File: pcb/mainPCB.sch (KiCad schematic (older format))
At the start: 31 parts, among them J1 Inputs, J11 Conn_01x04_Male, J12 Conn_01x04_Male, J2 ESP32_left, J3 ESP32_right, J4 F9P_left_top, J5 F9P left bottom, J6 F9P right, J7 Motor A, J8 Motor B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

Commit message: first version of the new feature set
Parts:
- removed C1: 100n, symbol Device:C
- removed C10: 10u, symbol Device:C
- removed C14: 470u, symbol Device:CP
- removed J1: Inputs, symbol Connector:Screw_Terminal_01x08
- removed J11, J12: Conn_01x04_Male, symbol Connector:Conn_01x04_Male
- removed J2: ESP32_left, symbol Connector:Conn_01x15_Female
- removed J3: ESP32_right, symbol Connector:Conn_01x15_Female
- removed J4: F9P_left_top, symbol Connector:Conn_01x08_Female
- removed J5: F9P left bottom, symbol Connector:Conn_01x08_Female
- removed J6: F9P right, symbol Connector:Conn_01x08_Female
- removed J7: Motor A, symbol Connector:Screw_Terminal_01x02
- removed J8: Motor B, symbol Connector:Screw_Terminal_01x02
- removed J9: Power, symbol Connector:Screw_Terminal_01x02
- removed U1: MMA8452Q, symbol Sensor_Motion_own:MMA8452Q
- added C5: 22u, Capacitor_SMD:C_0805_2012Metric, symbol Device:C
- added D3: LED/green, Capacitor_SMD:C_0805_2012Metric, symbol Device:LED
- added D4: LED/red, Capacitor_SMD:C_0805_2012Metric, symbol Device:LED
- added H6, H7, H8: MountingHole, MountingHole:MountingHole_3.2mm_M3_DIN965, symbol Mechanical:MountingHole
- added IC1: FXL6408UMX, ICs_own:QFN40P180X260X55-16N, symbol Interface_Expansion_own:FXL6408UMX
- added J1: PTSM-Header-Horizontal-6, Connector_own:1814883, symbol Connector_own:PTSM-Header-Horizontal-6
- added J3: PTSM-Header-Horizontal-7, Connector_own:1814896, symbol Connector_own:PTSM-Header-Horizontal-7
- added J4: CCA-Header-Horizontal-4, Connector_own:1836366, symbol Connector_own:CCA-Header-Horizontal-4
- added R10, R6: 47k, Resistor_SMD:R_0805_2012Metric, symbol Device:R
- added R11, R12, R13, R7, R8, R9: 1k, Resistor_SMD:R_0805_2012Metric, symbol Device:R
- added SW1: SW_Push, Button_Switch_SMD:SW_SPST_PTS645, symbol Switch:SW_Push
- added U1: ESP32-WROOM-32, RF_Module:ESP32-WROOM-32, symbol RF_Module:ESP32-WROOM-32
- C1: renamed from C11; value 22n -> 100n; footprint (none) -> Capacitor_SMD:C_0805_2012Metric
- C2: value 4.7u -> 100n; footprint (none) -> Capacitor_SMD:C_0805_2012Metric
- C3: footprint (none) -> Capacitor_SMD:C_0805_2012Metric
- C4: value 22u -> 100n; footprint (none) -> Capacitor_SMD:C_0805_2012Metric
- D1: value Network -> LED/blue; footprint (none) -> Capacitor_SMD:C_0805_2012Metric
- D2: value NTRIP -> LED/blue; footprint (none) -> Capacitor_SMD:C_0805_2012Metric
- H1: renamed from H5; footprint (none) -> MountingHole:MountingHole_4.3mm_M4_DIN965
- H2: footprint (none) -> MountingHole:MountingHole_4.3mm_M4_DIN965
- H3: renamed from H4; footprint (none) -> MountingHole:MountingHole_4.3mm_M4_DIN965
- H4: renamed from H3; footprint (none) -> MountingHole:MountingHole_4.3mm_M4_DIN965
- H5: renamed from H1; footprint (none) -> MountingHole:MountingHole_3.2mm_M3_DIN965
- R1: value 47 -> 120; footprint (none) -> Resistor_SMD:R_0805_2012Metric
- R2, R3: value 160 -> 620; footprint (none) -> Resistor_SMD:R_0805_2012Metric
- R4, R5: value 4.7k -> 620; footprint (none) -> Resistor_SMD:R_0805_2012Metric
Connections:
- net labels added: CAN_RXD, CAN_TXD, ESP_EN, I2C_3_SCL, I2C_3_SDA, I2C_5_SCL, I2C_5_SDA, M1_INA, M1_INB, M1_PWM, M2_INA, M2_INB, M2_PWM, RXD01, RXD02, TXD01, TXD02
- net labels removed: +3.3V, CAN_RX, CAN_TX, I2C_SCL, I2C_SDA, VSPI_CLK, VSPI_CS0, VSPI_MISO, VSPI_MOSI
- wire segments 137 -> 187
- no-connect marks 31 -> 9
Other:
- note removed: "Extensions"
- moved on the sheet: C1, H1, H2, H3, H4, H5, R1

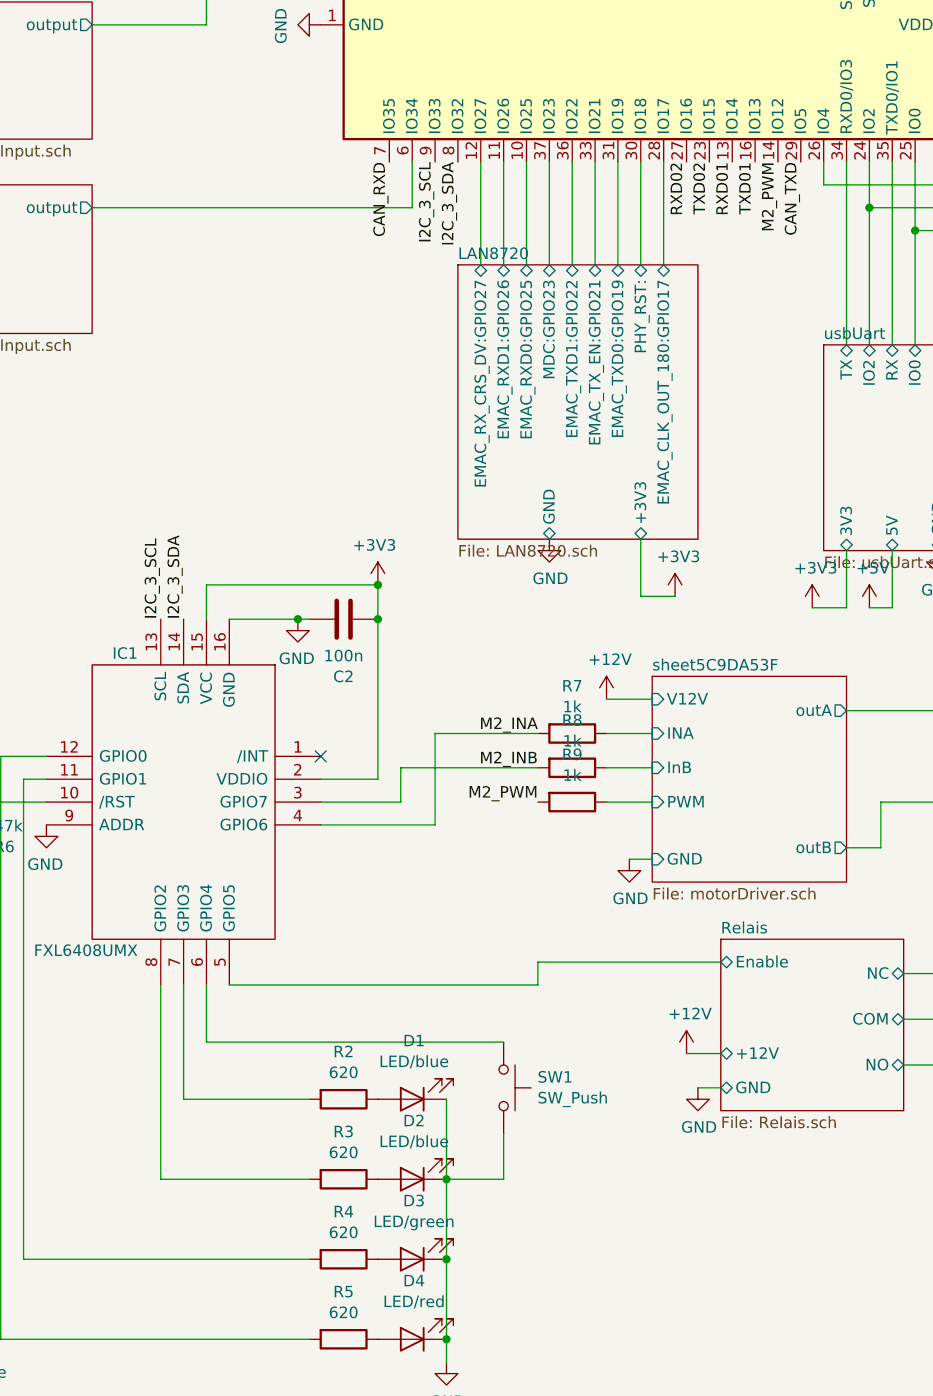
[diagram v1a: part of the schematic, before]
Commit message: changed connection of the LAN8720A, RST to the FXL6408 and MDIO to the ESP32 (where RST was before). fixes #2
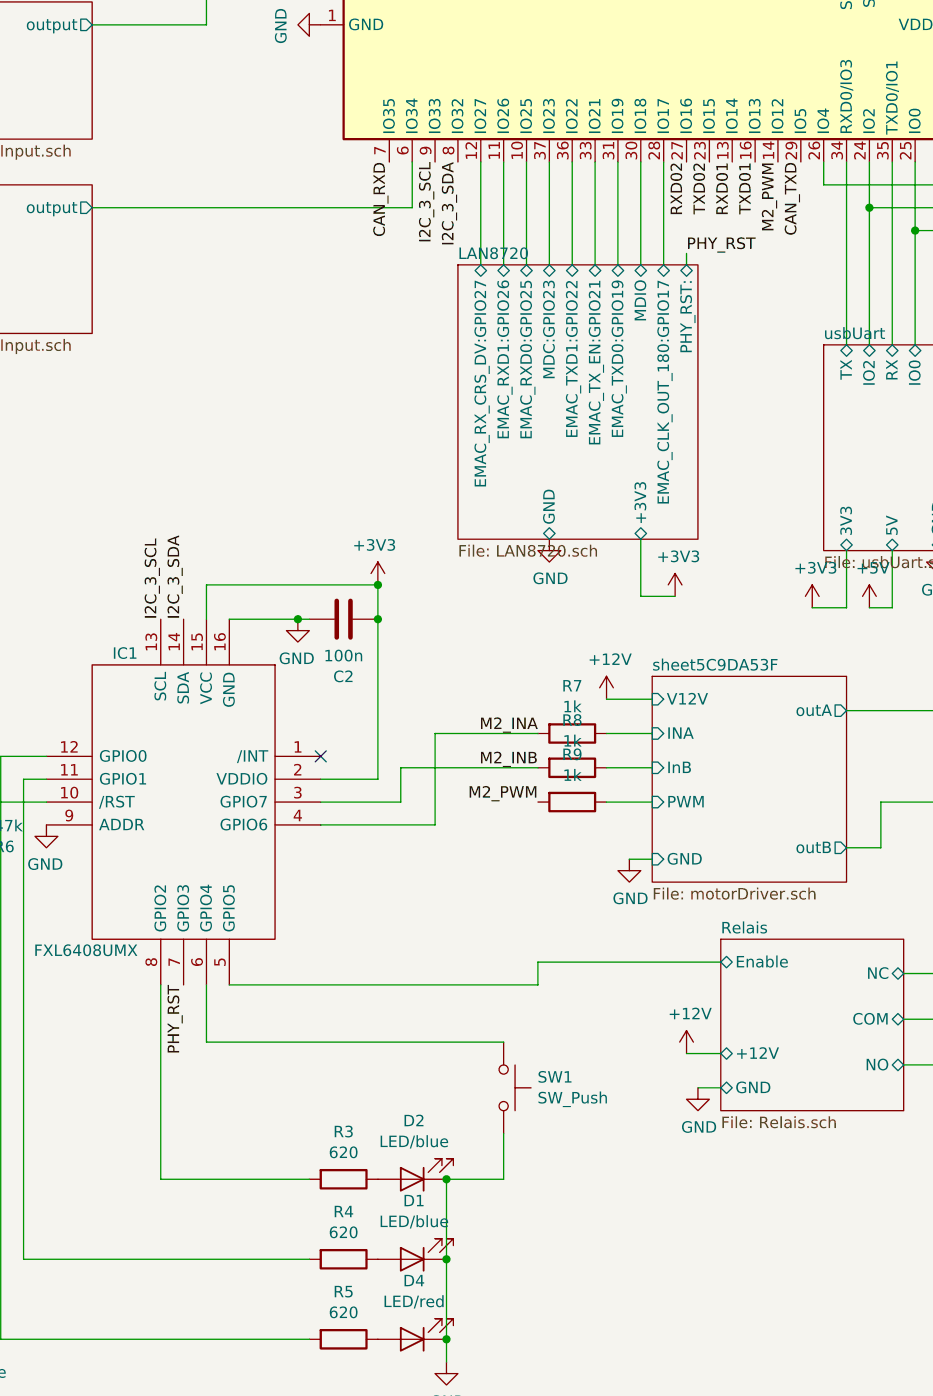
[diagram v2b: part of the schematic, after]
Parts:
- removed D1: LED/blue, Capacitor_SMD:C_0805_2012Metric, symbol Device:LED
- removed R2: 620, Resistor_SMD:R_0805_2012Metric, symbol Device:R
- D1: renamed from D3; value LED/green -> LED/blue
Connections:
- net PHY_RST: now reaches IC1.7 (GPIO3)
- net LAN8720/PHY_RST: renamed LAN8720/MDIO
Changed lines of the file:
@@
 	7100 4150 7000 4150
-$Comp
-L Device:R R2
-U 1 1 5CB615BA
-P 4700 6300
-F 0 "R2" V 4493 6300 50  0000 C CNN
-F 1 "620" V 4584 6300 50  0000 C CNN
-F 2 "Resistor_SMD:R_0805_2012Metric" V 4630 6300 50  0001 C CNN
-F 3 "~" H 4700 6300 50  0001 C CNN
-	1    4700 6300
-	0    1    1    0
-$EndComp
-$Comp
-L Device:LED D1
-U 1 1 5CB66F82
-P 5000 6300
-F 0 "D1" H 4992 6045 50  0000 C CNN
-F 1 "LED/blue" H 4992 6136 50  0000 C CNN
-F 2 "Capacitor_SMD:C_0805_2012Metric" H 5000 6300 50  0001 C CNN
-F 3 "~" H 5000 6300 50  0001 C CNN
-	1    5000 6300
-	-1   0    0    1
-$EndComp
 $Comp
 L Mechanical:MountingHole H8
@@
 F5 "EMAC_TX_EN:GPIO21" B T 5800 2650 50
 F6 "+3V3" B B 6000 3850 50
-F7 "PHY_RST:" B T 6000 2650 50
+F7 "PHY_RST:" B T 6200 2650 50
 F8 "MDC:GPIO23" B T 5600 2650 50
 F9 "GND" B B 5600 3850 50
@@
 F11 "EMAC_RXD0:GPIO25" B T 5500 2650 50
 F12 "EMAC_RXD1:GPIO26" B T 5400 2650 50
+F13 "MDIO" B T 6000 2650 50
 $EndSheet
 Wire Wire Line
@@
 Wire Wire Line
 	6100 2200 6100 2650
-Wire Wire Line
-	6000 2650 6000 2200
 Wire Wire Line
 	5900 2200 5900 2650
@@
 $EndComp
 $Comp
-L Device:LED D3
+L Device:LED D1
 U 1 1 5CF2F275
 P 5000 7000
-F 0 "D3" H 4992 6745 50  0000 C CNN
-F 1 "LED/green" H 4992 6836 50  0000 C CNN
+F 0 "D1" H 4992 6745 50  0000 C CNN
+F 1 "LED/blue" H 4992 6836 50  0000 C CNN
 F 2 "Capacitor_SMD:C_0805_2012Metric" H 5000 7000 50  0001 C CNN
 F 3 "~" H 5000 7000 50  0001 C CNN
@@
 	-1   0    0    1
 $EndComp
-Wire Wire Line
-	5150 6300 5150 6650
 Connection ~ 5150 6650
 Wire Wire Line
@@
 	1    0    0    -1
 $EndComp
-Wire Wire Line
-	4550 6300 4000 6300
 Wire Wire Line
 	3900 6650 4550 6650
@@
 	4100 5800 4100 6050
 Wire Wire Line
-	4000 5800 4000 6300
-Wire Wire Line
 	3900 5800 3900 6650
 Wire Wire Line
@@
 Wire Wire Line
 	5100 5100 4600 5100
+Wire Wire Line
+	6000 2200 6000 2650
+Text Label 4000 5800 3    50   ~ 0
+PHY_RST
+Text Label 6200 2600 0    50   ~ 0
+PHY_RST
+Wire Wire Line
+	6200 2600 6200 2650
 $EndSCHEMATC

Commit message: Added an other uart for ardusimple RTK2Bligh daughterboard on top of the normal RTK2B. Removed two LEDs to free up PINs
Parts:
- removed D1: LED/blue, Capacitor_SMD:C_0805_2012Metric, symbol Device:LED
- removed D4: LED/red, Capacitor_SMD:C_0805_2012Metric, symbol Device:LED
- removed R4, R5: 620, Resistor_SMD:R_0805_2012Metric, symbol Device:R
- added J2: Conn_01x02_Male, Connector_PinHeader_2.54mm:PinHeader_1x02_P2.54mm_Vertical, symbol Connector:Conn_01x02_Male
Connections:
- net M1_INA: now also IC1.4 (GPIO6); no longer U1.25 (IO0)
- net M1_INB: now also IC1.3 (GPIO7); no longer U1.24 (IO2)
- net M2_INA: now also IC1.6 (GPIO4); no longer IC1.4 (GPIO6)
- net M2_INB: now also IC1.5 (GPIO5); no longer IC1.3 (GPIO7)
- net PHY_RST: now also IC1.11 (GPIO1); no longer IC1.7 (GPIO3)
- net Relais/Enable: now also IC1.7 (GPIO3); no longer IC1.5 (GPIO5)
- net at SW1.1: now also IC1.12 (GPIO0); no longer IC1.6 (GPIO4)
- new net RXD03: J2.2 (Pin_2), U1.24 (IO2)
- new net TXD03: J2.1 (Pin_1), U1.25 (IO0)
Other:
- moved on the sheet: SW1
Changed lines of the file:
@@
 	6800 2300 8800 2300
 Wire Wire Line
-	8800 2300 8800 5100
-Wire Wire Line
-	8700 2400 8700 5400
-Wire Wire Line
-	8700 5400 8750 5400
-Wire Wire Line
-	7200 2500 8600 2500
-Wire Wire Line
-	8600 2500 8600 5700
-Wire Wire Line
-	8600 5700 8700 5700
+	7200 2500 7900 2500
 Connection ~ 7200 2500
 Wire Wire Line
@@
 	-1   0    0    1
 $EndComp
-$Comp
-L Device:R R4
-U 1 1 5CF2F26E
-P 4700 7000
-F 0 "R4" V 4493 7000 50  0000 C CNN
-F 1 "620" V 4584 7000 50  0000 C CNN
-F 2 "Resistor_SMD:R_0805_2012Metric" V 4630 7000 50  0001 C CNN
-F 3 "~" H 4700 7000 50  0001 C CNN
-	1    4700 7000
-	0    1    1    0
-$EndComp
-$Comp
-L Device:LED D1
-U 1 1 5CF2F275
-P 5000 7000
-F 0 "D1" H 4992 6745 50  0000 C CNN
-F 1 "LED/blue" H 4992 6836 50  0000 C CNN
-F 2 "Capacitor_SMD:C_0805_2012Metric" H 5000 7000 50  0001 C CNN
-F 3 "~" H 5000 7000 50  0001 C CNN
-	1    5000 7000
-	-1   0    0    1
-$EndComp
-$Comp
-L Device:R R5
-U 1 1 5CF379C3
-P 4700 7350
-F 0 "R5" V 4493 7350 50  0000 C CNN
-F 1 "620" V 4584 7350 50  0000 C CNN
-F 2 "Resistor_SMD:R_0805_2012Metric" V 4630 7350 50  0001 C CNN
-F 3 "~" H 4700 7350 50  0001 C CNN
-	1    4700 7350
-	0    1    1    0
-$EndComp
-$Comp
-L Device:LED D4
-U 1 1 5CF379CA
-P 5000 7350
-F 0 "D4" H 4992 7095 50  0000 C CNN
-F 1 "LED/red" H 4992 7186 50  0000 C CNN
-F 2 "Capacitor_SMD:C_0805_2012Metric" H 5000 7350 50  0001 C CNN
-F 3 "~" H 5000 7350 50  0001 C CNN
-	1    5000 7350
-	-1   0    0    1
-$EndComp
-Connection ~ 5150 6650
-Wire Wire Line
-	5150 6650 5150 7000
-Connection ~ 5150 7000
-Wire Wire Line
-	5150 7000 5150 7350
-Connection ~ 5150 7350
-Wire Wire Line
-	5150 7350 5150 7450
-$Comp
-L power:GND #PWR018
-U 1 1 5CF489F6
-P 5150 7450
-F 0 "#PWR018" H 5150 7200 50  0001 C CNN
-F 1 "GND" H 5155 7277 50  0000 C CNN
-F 2 "" H 5150 7450 50  0001 C CNN
-F 3 "" H 5150 7450 50  0001 C CNN
-	1    5150 7450
-	1    0    0    -1
-$EndComp
 Wire Wire Line
 	3900 6650 4550 6650
@@
 L Switch:SW_Push SW1
 U 1 1 5CB659C5
-P 5400 6250
-F 0 "SW1" V 5354 6398 50  0000 L CNN
-F 1 "SW_Push" V 5445 6398 50  0000 L CNN
-F 2 "Button_Switch_SMD:SW_SPST_PTS645" H 5400 6450 50  0001 C CNN
-F 3 "" H 5400 6450 50  0001 C CNN
-	1    5400 6250
-	0    1    1    0
-$EndComp
-Wire Wire Line
-	5400 6450 5400 6650
+P 3050 5550
+F 0 "SW1" H 3004 5698 50  0000 L CNN
+F 1 "SW_Push" H 2900 5450 50  0000 L CNN
+F 2 "Button_Switch_SMD:SW_SPST_PTS645" H 3050 5750 50  0001 C CNN
+F 3 "" H 3050 5750 50  0001 C CNN
+	1    3050 5550
+	1    0    0    -1
+$EndComp
 $Sheet
 S 1500 5350 750  550
@@
 	5400 6650 5150 6650
 Wire Wire Line
-	5400 6050 4100 6050
-Wire Wire Line
 	6900 2200 6900 3000
 Wire Wire Line
-	7000 2400 8700 2400
+	7000 2400 8000 2400
 Connection ~ 7000 2400
 Wire Wire Line
@@
 	4850 4200 4850 4900
 Wire Wire Line
-	4950 4850 5550 4850
-Wire Wire Line
-	4200 5800 5550 5800
-Wire Wire Line
-	5550 5700 5550 5800
-Wire Wire Line
-	4100 5800 4100 6050
-Wire Wire Line
 	3900 5800 3900 6650
 Wire Wire Line
-	3400 4900 3300 4900
-Wire Wire Line
-	3300 4900 3300 7000
-Wire Wire Line
-	3300 7000 4550 7000
-Wire Wire Line
-	3200 7350 3200 4800
-Wire Wire Line
-	3200 4800 3400 4800
-Wire Wire Line
-	3200 7350 4550 7350
-Wire Wire Line
-	4950 4850 4950 5000
-Wire Wire Line
-	4950 5000 4600 5000
-Wire Wire Line
-	5550 4700 5100 4700
-Wire Wire Line
-	5100 4700 5100 5100
-Wire Wire Line
-	5100 5100 4600 5100
-Wire Wire Line
 	6000 2200 6000 2650
-Text Label 4000 5800 3    50   ~ 0
+Text Label 3400 4900 2    50   ~ 0
 PHY_RST
 Text Label 6200 2600 0    50   ~ 0
@@
 Wire Wire Line
 	6200 2600 6200 2650
+$Comp
+L power:GND #PWR018
+U 1 1 5CF489F6
+P 5400 6650
+F 0 "#PWR018" H 5400 6400 50  0001 C CNN
+F 1 "GND" H 5405 6477 50  0000 C CNN
+F 2 "" H 5400 6650 50  0001 C CNN
+F 3 "" H 5400 6650 50  0001 C CNN
+	1    5400 6650
+	1    0    0    -1
+$EndComp
+$Comp
+L power:GND #PWR07
+U 1 1 5CF41B3E
+P 3250 5550
+F 0 "#PWR07" H 3250 5300 50  0001 C CNN
+F 1 "GND" H 3255 5377 50  0000 C CNN
+F 2 "" H 3250 5550 50  0001 C CNN
+F 3 "" H 3250 5550 50  0001 C CNN
+	1    3250 5550
+	1    0    0    -1
+$EndComp
+Wire Wire Line
+	2800 5550 2850 5550
+Wire Wire Line
+	4000 5800 4000 6200
+Wire Wire Line
+	4000 6200 5550 6200
+Wire Wire Line
+	5550 6200 5550 5700
+Text Label 4600 5000 0    50   ~ 0
+M1_INB
+Text Label 4600 5100 0    50   ~ 0
+M1_INA
+Text Label 7500 2400 0    50   ~ 0
+RXD03
+Text Label 7500 2500 0    50   ~ 0
+TXD03
+Wire Wire Line
+	8800 2300 8800 5100
+$Comp
+L Connector:Conn_01x02_Male J2
+U 1 1 5CF972CB
+P 7900 2750
+F 0 "J2" V 8053 2563 50  0000 R CNN
+F 1 "Conn_01x02_Male" V 7962 2563 50  0000 R CNN
+F 2 "Connector_PinHeader_2.54mm:PinHeader_1x02_P2.54mm_Vertical" H 7900 2750 50  0001 C CNN
+F 3 "~" H 7900 2750 50  0001 C CNN
+	1    7900 2750
+	0    -1   -1   0
+$EndComp
+Wire Wire Line
+	7900 2550 7900 2500
+Wire Wire Line
+	8000 2550 8000 2400
+Text Label 4100 5800 3    50   ~ 0
+M2_INA
+Text Label 4200 5800 3    50   ~ 0
+M2_INB
+Wire Wire Line
+	2800 4800 3400 4800
+Wire Wire Line
+	2800 4800 2800 5550
 $EndSCHEMATC

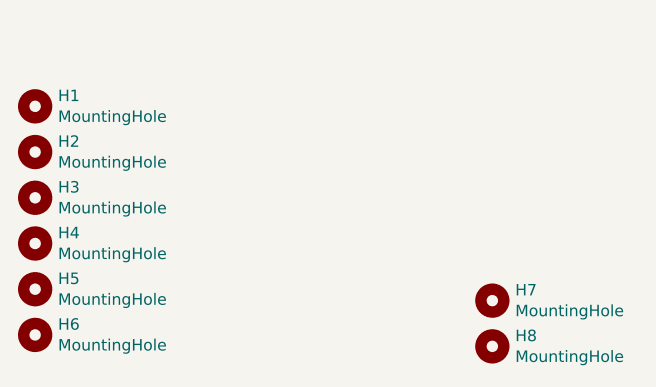
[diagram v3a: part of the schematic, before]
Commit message: Pull FORCEON to high on RS232 to avoid standby, fixed #18. Also implemented virtual symbol for permanent fiducials
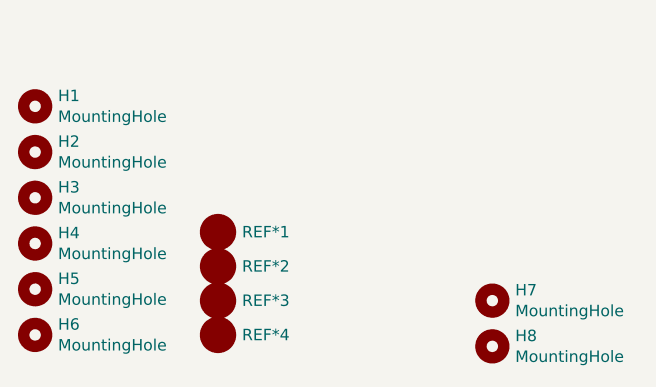
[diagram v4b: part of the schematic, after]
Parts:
- added REF*1, REF*2, REF*3, REF*4: Fiducial, Fiducial:Fiducial_1mm_Dia_2mm_Outer, symbol Virtual_own:Fiducial
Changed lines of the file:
@@
 Wire Wire Line
 	2800 4800 2800 5550
+$Comp
+L Virtual_own:Fiducial REF*4
+U 1 1 5D4DF8B0
+P 1600 7650
+F 0 "REF*4" H 1555 7700 50  0000 L CNN
+F 1 "Fiducial" H 1600 7700 50  0001 C CNN
+F 2 "Fiducial:Fiducial_1mm_Dia_2mm_Outer" H 1600 7650 50  0001 C CNN
+F 3 "" H 1600 7650 50  0001 C CNN
+	1    1600 7650
+	1    0    0    -1
+$EndComp
+$Comp
+L Virtual_own:Fiducial REF*3
+U 1 1 5D4DF928
+P 1600 7500
+F 0 "REF*3" H 1555 7550 50  0000 L CNN
+F 1 "Fiducial" H 1600 7550 50  0001 C CNN
+F 2 "Fiducial:Fiducial_1mm_Dia_2mm_Outer" H 1600 7500 50  0001 C CNN
+F 3 "" H 1600 7500 50  0001 C CNN
+	1    1600 7500
+	1    0    0    -1
+$EndComp
+$Comp
+L Virtual_own:Fiducial REF*2
+U 1 1 5D4DF980
+P 1600 7350
+F 0 "REF*2" H 1555 7400 50  0000 L CNN
+F 1 "Fiducial" H 1600 7400 50  0001 C CNN
+F 2 "Fiducial:Fiducial_1mm_Dia_2mm_Outer" H 1600 7350 50  0001 C CNN
+F 3 "" H 1600 7350 50  0001 C CNN
+	1    1600 7350
+	1    0    0    -1
+$EndComp
+$Comp
+L Virtual_own:Fiducial REF*1
+U 1 1 5D4DF9D6
+P 1600 7200
+F 0 "REF*1" H 1555 7250 50  0000 L CNN
+F 1 "Fiducial" H 1600 7250 50  0001 C CNN
+F 2 "Fiducial:Fiducial_1mm_Dia_2mm_Outer" H 1600 7200 50  0001 C CNN
+F 3 "" H 1600 7200 50  0001 C CNN
+	1    1600 7200
+	1    0    0    -1
+$EndComp
 $EndSCHEMATC
